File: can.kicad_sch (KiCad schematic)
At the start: 13 parts, among them U6 TJA1051T/3

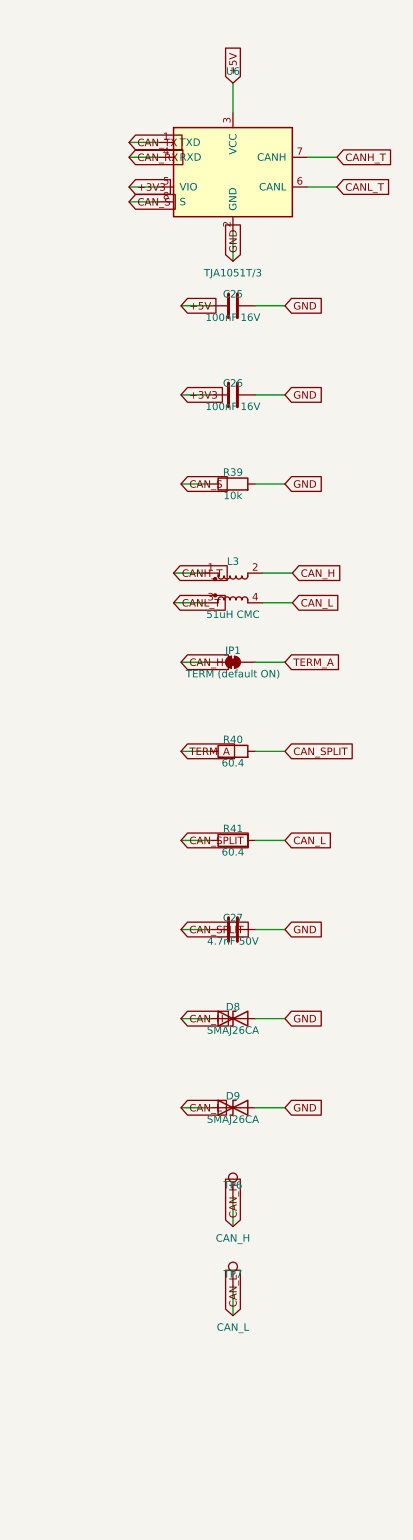
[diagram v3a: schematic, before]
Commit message: Add WS2812 5V DIN, SPI breakout, and PCB handoff docs.
Shift-light header uses a 74AHCT1G125 so GPIO48 drives real 5V data; SPI lands on IO40/41/42/47 with spare IO3/45/46 kept. README §10 covers remaining routing for the next agent.

Co-authored-by: Cursor <cursoragent@cursor.com>
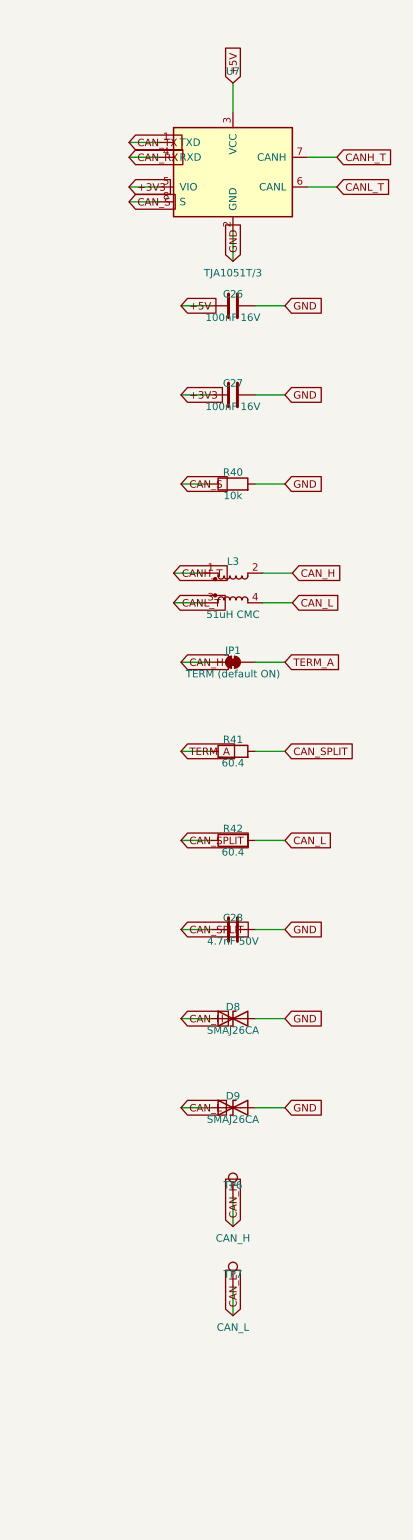
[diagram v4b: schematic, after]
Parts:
- removed C25: 100nF 16V, Capacitor_SMD:C_0805_2012Metric, symbol Device:C
- removed R39: 10k, Resistor_SMD:R_0805_2012Metric, symbol Device:R
- removed U6: TJA1051T/3, Package_SO:SOIC-8_3.9x4.9mm_P1.27mm, symbol Interface_CAN_LIN:TJA1051T-3
- added C28: 4.7nF 50V, Capacitor_SMD:C_0805_2012Metric, symbol Device:C
- added R42: 60.4, Resistor_SMD:R_0805_2012Metric, symbol Device:R
- added U7: TJA1051T/3, Package_SO:SOIC-8_3.9x4.9mm_P1.27mm, symbol Interface_CAN_LIN:TJA1051T-3
- C27: value 4.7nF 50V -> 100nF 16V; Note Split-termination common-mode stabiliser -> (none)
- R40: value 60.4 -> 10k; Note Split termination upper half -> Default to normal (non-silent) mode
- R41: Note Split termination lower half -> Split termination upper half
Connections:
- net +3V3: now also C27.1, U7.5 (VIO); no longer C26.1
- net +5V: now also C26.1, U7.3 (VCC)
- net CANH_T: now also U7.7 (CANH)
- net CANL_T: now also U7.6 (CANL)
- net CAN_L: now also R42.2; no longer R41.2
- net CAN_RX: now also U7.4 (RXD)
- net CAN_S: now also R40.1, U7.8 (S)
- net CAN_SPLIT: now also R41.2, C28.1, R42.1; no longer C27.1, R40.2, R41.1
- net CAN_TX: now also U7.1 (TXD)
- net GND: now also R40.2, C28.2, U7.2 (GND)
- net TERM_A: now also R41.1; no longer R40.1
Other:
- moved on the sheet: C26, C27, R40, R41
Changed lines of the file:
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@@
   (symbol (lib_id "Interface_CAN_LIN:TJA1051T-3") (at 59.69 33.02 0) (unit 1)
     (in_bom yes) (on_board yes) (dnp no)
-    (property "Reference" "U6" (at 59.69 15.78 0)
+    (property "Reference" "U7" (at 59.69 15.78 0)
       (effects (font (size 1.27 1.27)) )
     )
@@
     (instances
       (project "esp32s3-can-sd-logger"
-        (path "/3276c6e6-7085-5954-8442-c6cef7eab316/de4828a4-9871-500a-b45f-afe12f432271" (reference "U6") (unit 1))
+        (path "/3276c6e6-7085-5954-8442-c6cef7eab316/de4828a4-9871-500a-b45f-afe12f432271" (reference "U7") (unit 1))
       )
     )
@@
   (symbol (lib_id "Device:C") (at 59.69 55.88 90) (unit 1)
     (in_bom yes) (on_board yes) (dnp no)
-    (property "Reference" "C25" (at 59.69 53.88 270)
+    (property "Reference" "C26" (at 59.69 53.88 270)
       (effects (font (size 1.27 1.27)) )
     )
@@
     (instances
       (project "esp32s3-can-sd-logger"
-        (path "/3276c6e6-7085-5954-8442-c6cef7eab316/de4828a4-9871-500a-b45f-afe12f432271" (reference "C25") (unit 1))
+        (path "/3276c6e6-7085-5954-8442-c6cef7eab316/de4828a4-9871-500a-b45f-afe12f432271" (reference "C26") (unit 1))
       )
     )
@@
   (symbol (lib_id "Device:C") (at 59.69 71.12 90) (unit 1)
     (in_bom yes) (on_board yes) (dnp no)
-    (property "Reference" "C26" (at 59.69 69.12 270)
+    (property "Reference" "C27" (at 59.69 69.12 270)
       (effects (font (size 1.27 1.27)) )
     )
@@
     (instances
       (project "esp32s3-can-sd-logger"
-        (path "/3276c6e6-7085-5954-8442-c6cef7eab316/de4828a4-9871-500a-b45f-afe12f432271" (reference "C26") (unit 1))
+        (path "/3276c6e6-7085-5954-8442-c6cef7eab316/de4828a4-9871-500a-b45f-afe12f432271" (reference "C27") (unit 1))
       )
     )
@@
   (symbol (lib_id "Device:R") (at 59.69 86.36 90) (unit 1)
     (in_bom yes) (on_board yes) (dnp no)
-    (property "Reference" "R39" (at 59.69 84.36 270)
+    (property "Reference" "R40" (at 59.69 84.36 270)
       (effects (font (size 1.27 1.27)) )
     )
@@
     (instances
       (project "esp32s3-can-sd-logger"
-        (path "/3276c6e6-7085-5954-8442-c6cef7eab316/de4828a4-9871-500a-b45f-afe12f432271" (reference "R39") (unit 1))
+        (path "/3276c6e6-7085-5954-8442-c6cef7eab316/de4828a4-9871-500a-b45f-afe12f432271" (reference "R40") (unit 1))
       )
     )
@@
   (symbol (lib_id "Device:R") (at 59.69 132.08 90) (unit 1)
     (in_bom yes) (on_board yes) (dnp no)
-    (property "Reference" "R40" (at 59.69 130.08 270)
+    (property "Reference" "R41" (at 59.69 130.08 270)
       (effects (font (size 1.27 1.27)) )
     )
@@
     (instances
       (project "esp32s3-can-sd-logger"
-        (path "/3276c6e6-7085-5954-8442-c6cef7eab316/de4828a4-9871-500a-b45f-afe12f432271" (reference "R40") (unit 1))
+        (path "/3276c6e6-7085-5954-8442-c6cef7eab316/de4828a4-9871-500a-b45f-afe12f432271" (reference "R41") (unit 1))
       )
     )
@@
   (symbol (lib_id "Device:R") (at 59.69 147.32 90) (unit 1)
     (in_bom yes) (on_board yes) (dnp no)
-    (property "Reference" "R41" (at 59.69 145.32 270)
+    (property "Reference" "R42" (at 59.69 145.32 270)
       (effects (font (size 1.27 1.27)) )
     )
@@
     (instances
       (project "esp32s3-can-sd-logger"
-        (path "/3276c6e6-7085-5954-8442-c6cef7eab316/de4828a4-9871-500a-b45f-afe12f432271" (reference "R41") (unit 1))
+        (path "/3276c6e6-7085-5954-8442-c6cef7eab316/de4828a4-9871-500a-b45f-afe12f432271" (reference "R42") (unit 1))
       )
     )
@@
   (symbol (lib_id "Device:C") (at 59.69 162.56 90) (unit 1)
     (in_bom yes) (on_board yes) (dnp no)
-    (property "Reference" "C27" (at 59.69 160.56 270)
+    (property "Reference" "C28" (at 59.69 160.56 270)
       (effects (font (size 1.27 1.27)) )
     )
@@
     (instances
       (project "esp32s3-can-sd-logger"
-        (path "/3276c6e6-7085-5954-8442-c6cef7eab316/de4828a4-9871-500a-b45f-afe12f432271" (reference "C27") (unit 1))
-      )
-    )
+        (path "/3276c6e6-7085-5954-8442-c6cef7eab316/de4828a4-9871-500a-b45f-afe12f432271" (reference "C28") (unit 1))
+      )
+    )

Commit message: Schematic: power symbols and readable text placement (items 1-2 of 5)
The schematic was a netlist drawn as a picture: 486 global labels for 108
nets, roughly four per net, every part an island with a name flag on each
pin and no wires between anything. You could not trace a circuit by eye.
That is a fair description of a document that fails at the one thing a
schematic is for, and it is on me -- the generator was built to produce a
correct netlist and the drawing was an afterthought.

Two of the five agreed fixes are in:

Rails are power symbols. GND, +3V3, +5V, +5VS, +VBAT, VBUS and SD_VDD now
carry a proper power symbol instead of a net-name label -- 190 of them,
taking the label count from 486 to 296. Where KiCad has no stock symbol
for a rail a generic one is instantiated with its Value overridden, which
is how KiCad names a power net; validate.py re-extracts through KiCad and
compares node-for-node, so a wrong guess there would fail the build rather
than quietly merge two rails. PWR_FLAG keeps a label: pairing it with a
power symbol makes an island of two symbols that declares a rail and
connects to nothing visible.

Text no longer collides. Labels were all justified left, so any label
pointing back at its own component ran its text over the body -- RON_5V
across R4, SW_5V across L1; they now justify away from the part.
Reference and value sat hard against the symbol, so a pin leaving the top
or bottom put its stub and power symbol straight through them: "LM5164
(5V)" printed through the GND symbol under U2. Both now clear the stub,
and the row height accounts for it so the clearance does not just push
the collision into the next row. Power symbol references are hidden, as
they are in every schematic.

Also fixed: the packer wrapped on height but never on width, so the power
sheet silently ran off the 420 mm page -- two symbols landed at x = 422.9
where ERC reported them unconnected and nothing else complained. It now
fails loudly.

Items 3-5 (real hierarchy, w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
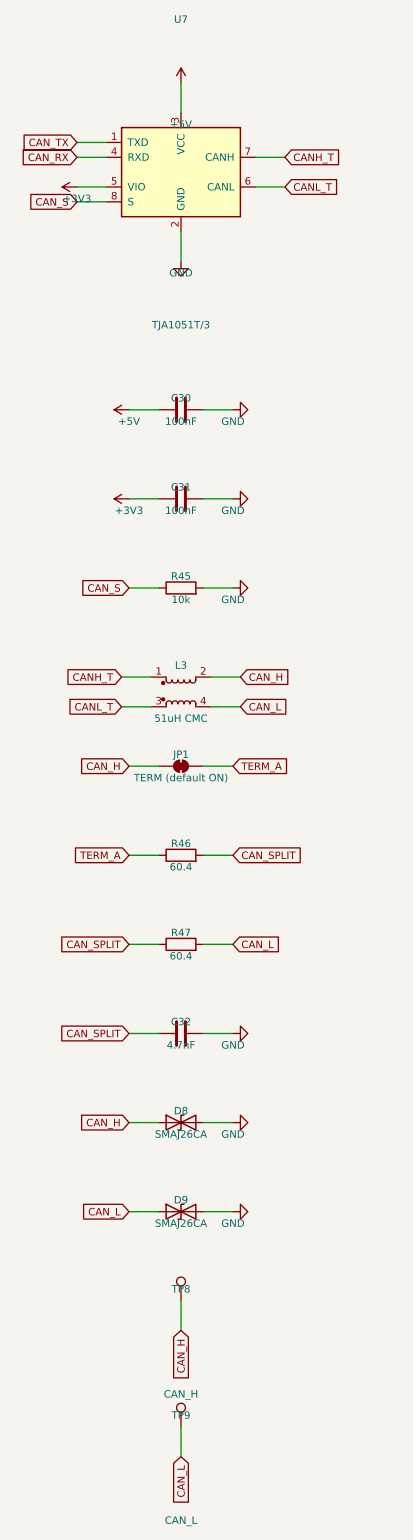
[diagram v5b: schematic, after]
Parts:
- removed C26, C27: 100nF 16V, Capacitor_SMD:C_0805_2012Metric, symbol Device:C
- removed C28: 4.7nF 50V, Capacitor_SMD:C_0805_2012Metric, symbol Device:C
- removed R40: 10k, Resistor_SMD:R_0805_2012Metric, symbol Device:R
- removed R41, R42: 60.4, Resistor_SMD:R_0805_2012Metric, symbol Device:R
- removed TP6: CAN_H, TestPoint:TestPoint_Pad_D1.5mm, symbol Connector:TestPoint
- removed TP7: CAN_L, TestPoint:TestPoint_Pad_D1.5mm, symbol Connector:TestPoint
- added C30, C31: 100nF, Capacitor_SMD:C_0805_2012Metric, symbol Device:C
- added C32: 4.7nF, Capacitor_SMD:C_0805_2012Metric, symbol Device:C
- added R45: 10k, Resistor_SMD:R_0805_2012Metric, symbol Device:R
- added R46, R47: 60.4, Resistor_SMD:R_0805_2012Metric, symbol Device:R
- added TP8: CAN_H, TestPoint:TestPoint_Pad_D1.5mm, symbol Connector:TestPoint
- added TP9: CAN_L, TestPoint:TestPoint_Pad_D1.5mm, symbol Connector:TestPoint
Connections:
- net +3V3: now also C31.1
- net +5V: now also C30.1
- net CAN_H: now also TP8.1
- net CAN_L: now also R47.2, TP9.1
- net CAN_S: now also R45.1
- net CAN_SPLIT: now also C32.1, R46.2, R47.1
- net GND: now also C30.2, C31.2, C32.2, R45.2
- net TERM_A: now also R46.1
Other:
- moved on the sheet: D8, D9, JP1, L3, U7

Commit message: Rev B is fully routed: zero DRC errors, nothing unconnected
84 x 84 mm, 1447 tracks, 258 vias, 179 footprints, 106 nets.

The last few connections were never routing problems. Each one was a part
sited away from the net it belongs to, and the autorouter reporting "no
path at any width" was telling the truth:

  +5VS  the sensor rail's source (PF1/FB2/D3) sat on the right beside the
        WS2812 header while everything it feeds -- the sensor harness and
        all four channel pull-ups -- is on the left. The net existed as
        two complete halves with a 45 mm gap through buck islands and the
        SD socket. Moved the source to the harness side.
  IO46  the strapping pull-downs were parked in the bottom band while
        IO3/IO45/IO46 run from the module's south pads to J7 at the top
        left, so R29 needed a trace the length of the board to reach its
        own net. Moved them under the module's south pads.

Adding router passes had never touched either. Moving the parts fixed
both immediately -- worth remembering next time a net "cannot be routed".

Also in this pass:

  - One LED. D6 (amber) and D7 (blue) and their resistors are gone; D4
    green stays on +3V3, which is the right rail to watch because it only
    lights if the whole chain came through -- battery, ideal diode, both
    converters. That also retires review item 11.2.10, the blue emitter
    that would have been near-invisible on a 3.288 V rail.
  - J7 grows to six pins: the three strapping pins, the two GPIOs freed
    by the LEDs (IO15/IO16), and a ground pin. The missing ground was
    review item 13.4.13.
  - USB_CC1 gets a Fine netclass at 0.2 mm. There is no route at 0.25 mm
    -- the USB-C pads are on 0.5 mm pitch and will not pass it -- and CC
    carries under a milliamp through a 5.1k pull-down.
  - build_board.py takes a lock. Two builds sharing the board file is how
    one run died at "Specctra session import failed" after ten minutes,
    when a second build regenerated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
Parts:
- removed D8, D9: SMAJ26CA, Diode_SMD:D_SMA, symbol Device:D_TVS
- removed R46, R47: 60.4, Resistor_SMD:R_0805_2012Metric, symbol Device:R
- added D6, D7: SMAJ26CA, Diode_SMD:D_SMA, symbol Device:D_TVS
- added R43: 10k, Resistor_SMD:R_0805_2012Metric, symbol Device:R
- added R44: 60.4, Resistor_SMD:R_0805_2012Metric, symbol Device:R
- R45: value 10k -> 60.4; Note Default to normal (non-silent) mode -> Split termination lower half
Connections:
- net CAN_H: now also D6.1 (A1)
- net CAN_L: now also R45.2, D7.1 (A1)
- net CAN_S: now also R43.1; no longer R45.1
- net CAN_SPLIT: now also R45.1, R44.2
- net GND: now also D6.2 (A2), D7.2 (A2), R43.2; no longer R45.2
- net TERM_A: now also R44.1
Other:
- moved on the sheet: R45
